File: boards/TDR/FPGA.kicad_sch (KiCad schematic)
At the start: 1 part, among them U1 LFE5UM5G-45-CABGA381

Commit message: change crystal footprint and roughly finish schematic
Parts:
- added U16: LFE5UM5G-25-CABGA381, symbol ECP5:LFE5UM5G-25-CABGA381
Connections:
- net VCCIO7 is gone; now on net +3V3: U1.H6 (VCCIO7), U1.H7 (VCCIO7), U1.J6 (VCCIO7)
- net D0: now also U1.C2 (PL23D)
- net D1: now also U1.B1 (PL23B)
- net D2: now also U1.B2 (PL23C)
- net D3: now also U1.A2 (PL23A)
- net D4: now also U1.B3 (PL14D)
- net D5: now also U1.A3 (PL14C)
- net D6: now also U1.B4 (PL14B)
- net D7: now also U1.A4 (PL11A)
- net RD#: now also U1.C5 (PL11D)
- net RXF#: now also U1.B5 (PL11C)
- net SIWU: now also U1.E5 (PL20C)
- net TXE#: now also U1.A5 (PL11B)
- net WR#: now also U1.D5 (PL17B)

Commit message: connect fpga vccio to 3.3V, add decoupling, route some tracks
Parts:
- removed U16: LFE5UM5G-25-CABGA381, symbol ECP5:LFE5UM5G-25-CABGA381
- added C21, C5: 100n, Capacitor_SMD:C_0402_1005Metric, symbol Device:C
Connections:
- net +3V3: now also C21.1, C5.1
- net GND: now also C21.2, C5.2
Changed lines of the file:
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@@
   (junction (at 53.34 133.35) (diameter 0) (color 0 0 0 0))
   (junction (at 54.61 140.97) (diameter 0) (color 0 0 0 0))
+  (junction (at 55.88 130.81) (diameter 0) (color 0 0 0 0))
   (junction (at 83.82 26.67) (diameter 0) (color 0 0 0 0))
   (junction (at 116.84 29.21) (diameter 0) (color 0 0 0 0))
@@
   (junction (at 185.42 29.21) (diameter 0) (color 0 0 0 0))
   (junction (at 217.17 29.21) (diameter 0) (color 0 0 0 0))
+  (junction (at 220.98 29.21) (diameter 0) (color 0 0 0 0))
   (wire (pts (xy 49.53 26.67) (xy 50.8 26.67))
     (stroke (width 0) (type solid) (color 0 0 0 0))
@@
     (stroke (width 0) (type solid) (color 0 0 0 0))
   )
+  (wire (pts (xy 55.88 130.81) (xy 59.69 130.81))
+    (stroke (width 0) (type solid) (color 0 0 0 0))
+  )
+  (wire (pts (xy 67.31 130.81) (xy 69.85 130.81))
+    (stroke (width 0) (type solid) (color 0 0 0 0))
+  )
+  (wire (pts (xy 69.85 130.81) (xy 69.85 131.445))
+    (stroke (width 0) (type solid) (color 0 0 0 0))
+  )
   (wire (pts (xy 82.55 26.67) (xy 83.82 26.67))
     (stroke (width 0) (type solid) (color 0 0 0 0))
@@
   )
   (wire (pts (xy 220.98 27.94) (xy 220.98 29.21))
+    (stroke (width 0) (type solid) (color 0 0 0 0))
+  )
+  (wire (pts (xy 220.98 29.21) (xy 225.425 29.21))
+    (stroke (width 0) (type solid) (color 0 0 0 0))
+  )
+  (wire (pts (xy 233.045 29.21) (xy 234.315 29.21))
+    (stroke (width 0) (type solid) (color 0 0 0 0))
+  )
+  (wire (pts (xy 234.315 29.21) (xy 234.315 29.845))
     (stroke (width 0) (type solid) (color 0 0 0 0))
   )
@@
     )
     (property "Datasheet" "" (id 3) (at 57.15 140.97 0)
+      (effects (font (size 1.27 1.27)) hide)
+    )
+  )
+  (symbol (lib_id "power:GND") (at 69.85 131.445 0) (unit 1)
+    (in_bom yes) (on_board yes)
+    (property "Reference" "#PWR0144" (id 0) (at 69.85 137.795 0)
+      (effects (font (size 1.27 1.27)) hide)
+    )
+    (property "Value" "GND" (id 1) (at 73.66 132.715 0))
+    (property "Footprint" "" (id 2) (at 69.85 131.445 0)
+      (effects (font (size 1.27 1.27)) hide)
+    )
+    (property "Datasheet" "" (id 3) (at 69.85 131.445 0)
+      (effects (font (size 1.27 1.27)) hide)
+    )
+  )
+  (symbol (lib_id "power:GND") (at 234.315 29.845 0) (unit 1)
+    (in_bom yes) (on_board yes)
+    (property "Reference" "#PWR0143" (id 0) (at 234.315 36.195 0)
+      (effects (font (size 1.27 1.27)) hide)
+    )
+    (property "Value" "GND" (id 1) (at 238.125 31.115 0))
+    (property "Footprint" "" (id 2) (at 234.315 29.845 0)
+      (effects (font (size 1.27 1.27)) hide)
+    )
+    (property "Datasheet" "" (id 3) (at 234.315 29.845 0)
+      (effects (font (size 1.27 1.27)) hide)
+    )
+  )
+  (symbol (lib_id "Device:C") (at 63.5 130.81 90) (unit 1)
+    (in_bom yes) (on_board yes)
+    (property "Reference" "C5" (id 0) (at 63.5 124.4408 90))
+    (property "Value" "100n" (id 1) (at 63.5 126.7395 90))
+    (property "Footprint" "Capacitor_SMD:C_0402_1005Metric" (id 2) (at 67.31 129.8448 0)
+      (effects (font (size 1.27 1.27)) hide)
+    )
+    (property "Datasheet" "~" (id 3) (at 63.5 130.81 0)
+      (effects (font (size 1.27 1.27)) hide)
+    )
+  )
+  (symbol (lib_id "Device:C") (at 229.235 29.21 90) (unit 1)
+    (in_bom yes) (on_board yes)
+    (property "Reference" "C21" (id 0) (at 229.235 22.8408 90))
+    (property "Value" "100n" (id 1) (at 229.235 25.1395 90))
+    (property "Footprint" "Capacitor_SMD:C_0402_1005Metric" (id 2) (at 233.045 28.2448 0)
+      (effects (font (size 1.27 1.27)) hide)
+    )
+    (property "Datasheet" "~" (id 3) (at 229.235 29.21 0)
       (effects (font (size 1.27 1.27)) hide)
     )
@@
     )
   )
-  (symbol (lib_id "ECP5:LFE5UM5G-25-CABGA381") (at 655.32 80.01 0) (unit 10)
-    (in_bom yes) (on_board yes)
-    (property "Reference" "U16" (id 0) (at 646.43 -71.12 0))
-    (property "Value" "LFE5UM5G-25-CABGA381" (id 1) (at 657.86 231.14 0))
-    (property "Footprint" "" (id 2) (at 655.32 80.01 0)
-      (effects (font (size 1.27 1.27)) hide)
-    )
-    (property "Datasheet" "" (id 3) (at 655.32 80.01 0)
-      (effects (font (size 1.27 1.27)) hide)
-    )
-  )
   (symbol (lib_id "ECP5:LFE5UM5G-45-CABGA381") (at 105.41 142.24 0) (unit 5)
     (in_bom yes) (on_board yes)
@@
     )
   )
-  (symbol (lib_id "ECP5:LFE5UM5G-25-CABGA381") (at 513.08 93.345 0) (unit 5)
-    (in_bom yes) (on_board yes)
-    (property "Reference" "U16" (id 0) (at 504.19 -57.785 0))
-    (property "Value" "LFE5UM5G-25-CABGA381" (id 1) (at 515.62 244.475 0))
-    (property "Footprint" "" (id 2) (at 513.08 93.345 0)
-      (effects (font (size 1.27 1.27)) hide)
-    )
-    (property "Datasheet" "" (id 3) (at 513.08 93.345 0)
-      (effects (font (size 1.27 1.27)) hide)
-    )
-  )
   (symbol (lib_id "ECP5:LFE5UM5G-45-CABGA381") (at 154.94 149.225 0) (unit 6)
     (in_bom yes) (on_board yes)
@@
     )
   )
-  (symbol (lib_id "ECP5:LFE5UM5G-25-CABGA381") (at 551.815 80.645 0) (unit 6)
-    (in_bom yes) (on_board yes)
-    (property "Reference" "U16" (id 0) (at 542.925 -70.485 0))
-    (property "Value" "LFE5UM5G-25-CABGA381" (id 1) (at 554.355 231.775 0))
-    (property "Footprint" "" (id 2) (at 551.815 80.645 0)
-      (effects (font (size 1.27 1.27)) hide)
-    )
-    (property "Datasheet" "" (id 3) (at 551.815 80.645 0)
-      (effects (font (size 1.27 1.27)) hide)
-    )
-  )
   (symbol (lib_id "ECP5:LFE5UM5G-45-CABGA381") (at 41.91 157.48 0) (unit 10)
     (in_bom yes) (on_board yes)
@@
     )
   )
-  (symbol (lib_id "ECP5:LFE5UM5G-25-CABGA381") (at 576.58 85.725 0) (unit 9)
-    (in_bom yes) (on_board yes)
-    (property "Reference" "U16" (id 0) (at 567.69 -65.405 0))
-    (property "Value" "LFE5UM5G-25-CABGA381" (id 1) (at 579.12 236.855 0))
-    (property "Footprint" "" (id 2) (at 576.58 85.725 0)
-      (effects (font (size 1.27 1.27)) hide)
-    )
-    (property "Datasheet" "" (id 3) (at 576.58 85.725 0)
-      (effects (font (size 1.27 1.27)) hide)
-    )
-  )
-  (symbol (lib_id "ECP5:LFE5UM5G-25-CABGA381") (at 386.08 86.995 0) (unit 1)
-    (in_bom yes) (on_board yes)
-    (property "Reference" "U16" (id 0) (at 377.19 -64.135 0))
-    (property "Value" "LFE5UM5G-25-CABGA381" (id 1) (at 388.62 238.125 0))
-    (property "Footprint" "" (id 2) (at 386.08 86.995 0)
-      (effects (font (size 1.27 1.27)) hide)
-    )
-    (property "Datasheet" "" (id 3) (at 386.08 86.995 0)
-      (effects (font (size 1.27 1.27)) hide)
-    )
-  )
   (symbol (lib_id "ECP5:LFE5UM5G-45-CABGA381") (at 39.37 63.5 0) (unit 1)
     (in_bom yes) (on_board yes)
@@
     )
   )
-  (symbol (lib_id "ECP5:LFE5UM5G-25-CABGA381") (at 361.95 92.075 0) (unit 2)
-    (in_bom yes) (on_board yes)
-    (property "Reference" "U16" (id 0) (at 353.06 -59.055 0))
-    (property "Value" "LFE5UM5G-25-CABGA381" (id 1) (at 364.49 243.205 0))
-    (property "Footprint" "" (id 2) (at 361.95 92.075 0)
-      (effects (font (size 1.27 1.27)) hide)
-    )
-    (property "Datasheet" "" (id 3) (at 361.95 92.075 0)
-      (effects (font (size 1.27 1.27)) hide)
-    )
-  )
   (symbol (lib_id "ECP5:LFE5UM5G-45-CABGA381") (at 72.39 71.12 0) (unit 2)
     (in_bom yes) (on_board yes)
@@
       (effects (font (size 1.27 1.27)) hide)
     )
-  )
-  (symbol (lib_id "ECP5:LFE5UM5G-25-CABGA381") (at 407.035 93.98 0) (unit 3)
-    (in_bom yes) (on_board yes)
-    (property "Reference" "U16" (id 0) (at 398.145 -57.15 0))
-    (property "Value" "LFE5UM5G-25-CABGA381" (id 1) (at 409.575 245.11 0))
-    (property "Footprint" "" (id 2) (at 407.035 93.98 0)
-      (effects (font (size 1.27 1.27)) hide)
-    )
-    (property "Datasheet" "" (id 3) (at 407.035 93.98 0)
-      (effects (font (size 1.27 1.27)) hide)
-    )
-  )
-  (symbol (lib_id "ECP5:LFE5UM5G-25-CABGA381") (at 423.545 93.98 0) (unit 4)
-    (in_bom yes) (on_board yes)
-    (property "Reference" "U16" (id 0) (at 414.655 -57.15 0))
-    (property "Value" "LFE5UM5G-25-CABGA381" (id 1) (at 426.085 245.11 0))
-    (property "Footprint" "" (id 2) (at 423.545 93.98 0)
-      (effects (font (size 1.27 1.27)) hide)
-    )
-    (property "Datasheet" "" (id 3) (at 423.545 93.98 0)
-      (effects (font (size 1.27 1.27)) hide)
-    )
-  )
-  (symbol (lib_id "ECP5:LFE5UM5G-25-CABGA381") (at 447.04 94.615 0) (unit 7)
-    (in_bom yes) (on_board yes)
-    (property "Reference" "U16" (id 0) (at 438.15 -56.515 0))
-    (property "Value" "LFE5UM5G-25-CABGA381" (id 1) (at 449.58 245.745 0))
-    (property "Footprint" "" (id 2) (at 447.04 94.615 0)
-      (effects (font (size 1.27 1.27)) hide)
-    )
-    (property "Datasheet" "" (id 3) (at 447.04 94.615 0)
-      (effects (font (size 1.27 1.27)) hide)
-    )
-  )
-  (symbol (lib_id "ECP5:LFE5UM5G-25-CABGA381") (at 473.71 86.36 0) (unit 8)
-    (in_bom yes) (on_board yes)
-    (property "Reference" "U16" (id 0) (at 464.82 -64.77 0))
-    (property "Value" "LFE5UM5G-25-CABGA381" (id 1) (at 476.25 237.49 0))
-    (property "Footprint" "" (id 2) (at 473.71 86.36 0)
-      (effects (font (size 1.27 1.27)) hide)
-    )
-    (property "Datasheet" "" (id 3) (at 473.71 86.36 0)
-      (effects (font (size 1.27 1.27)) hide)
-    )

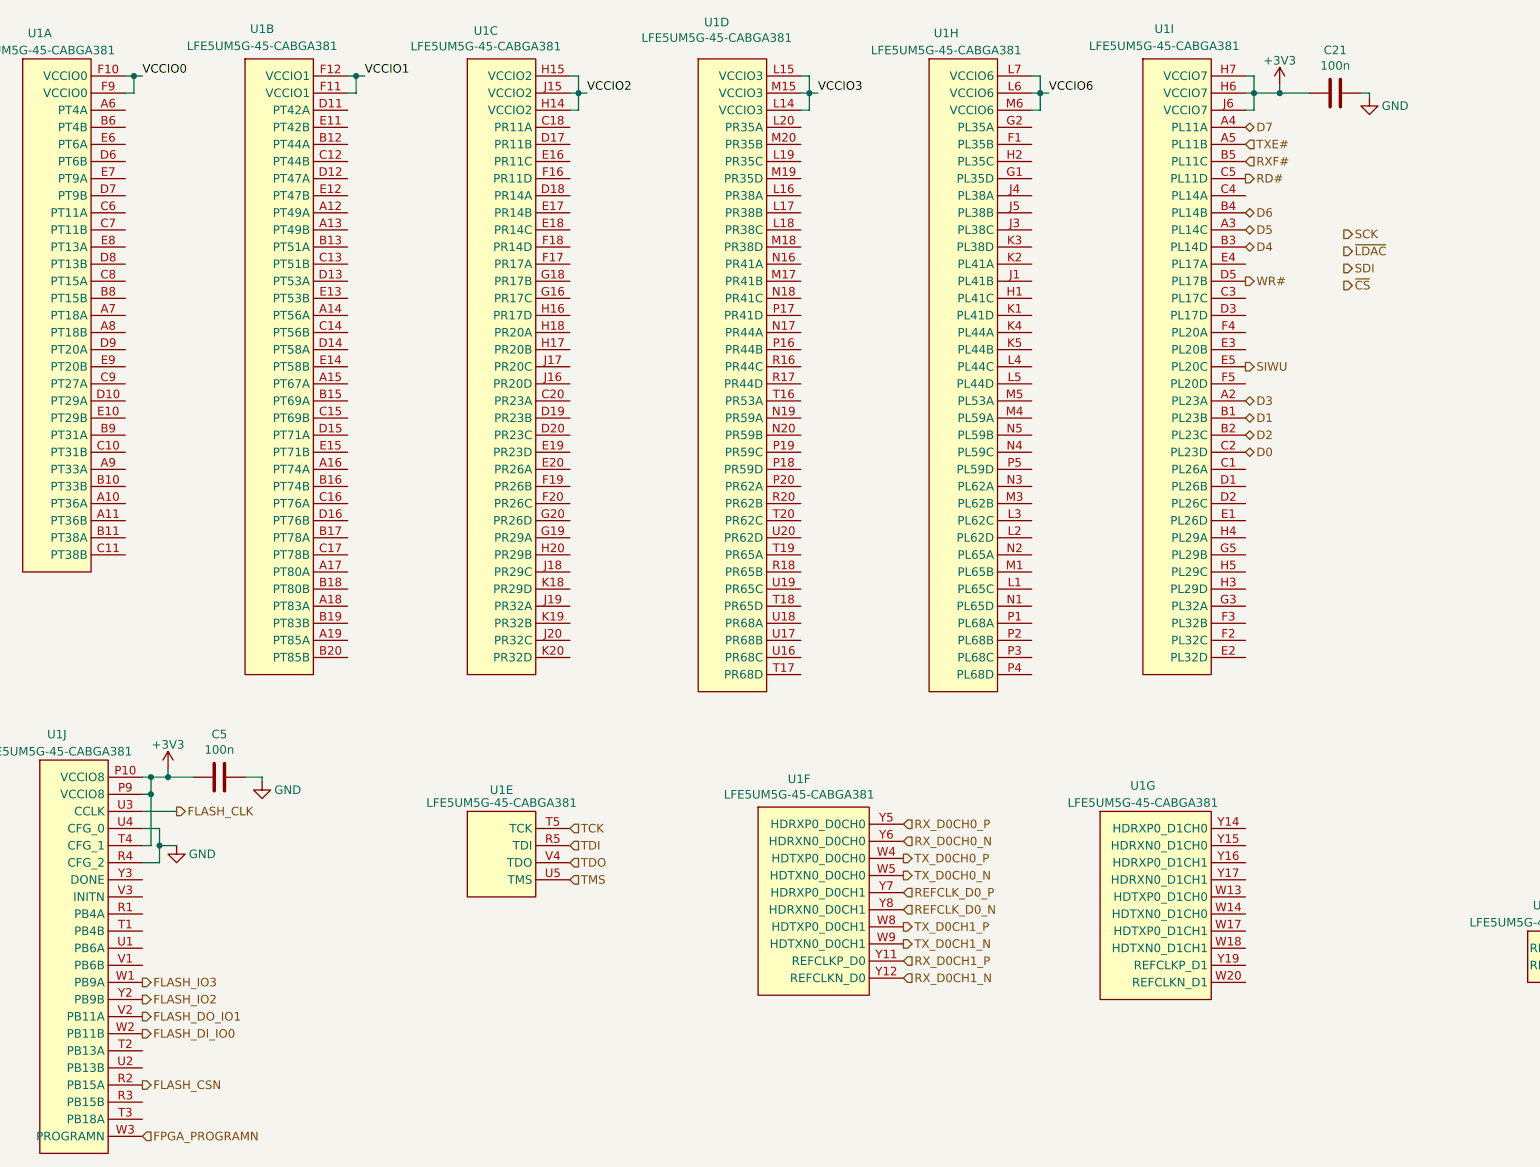
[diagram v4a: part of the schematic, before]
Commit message: solved DRC errors and routed few more nets
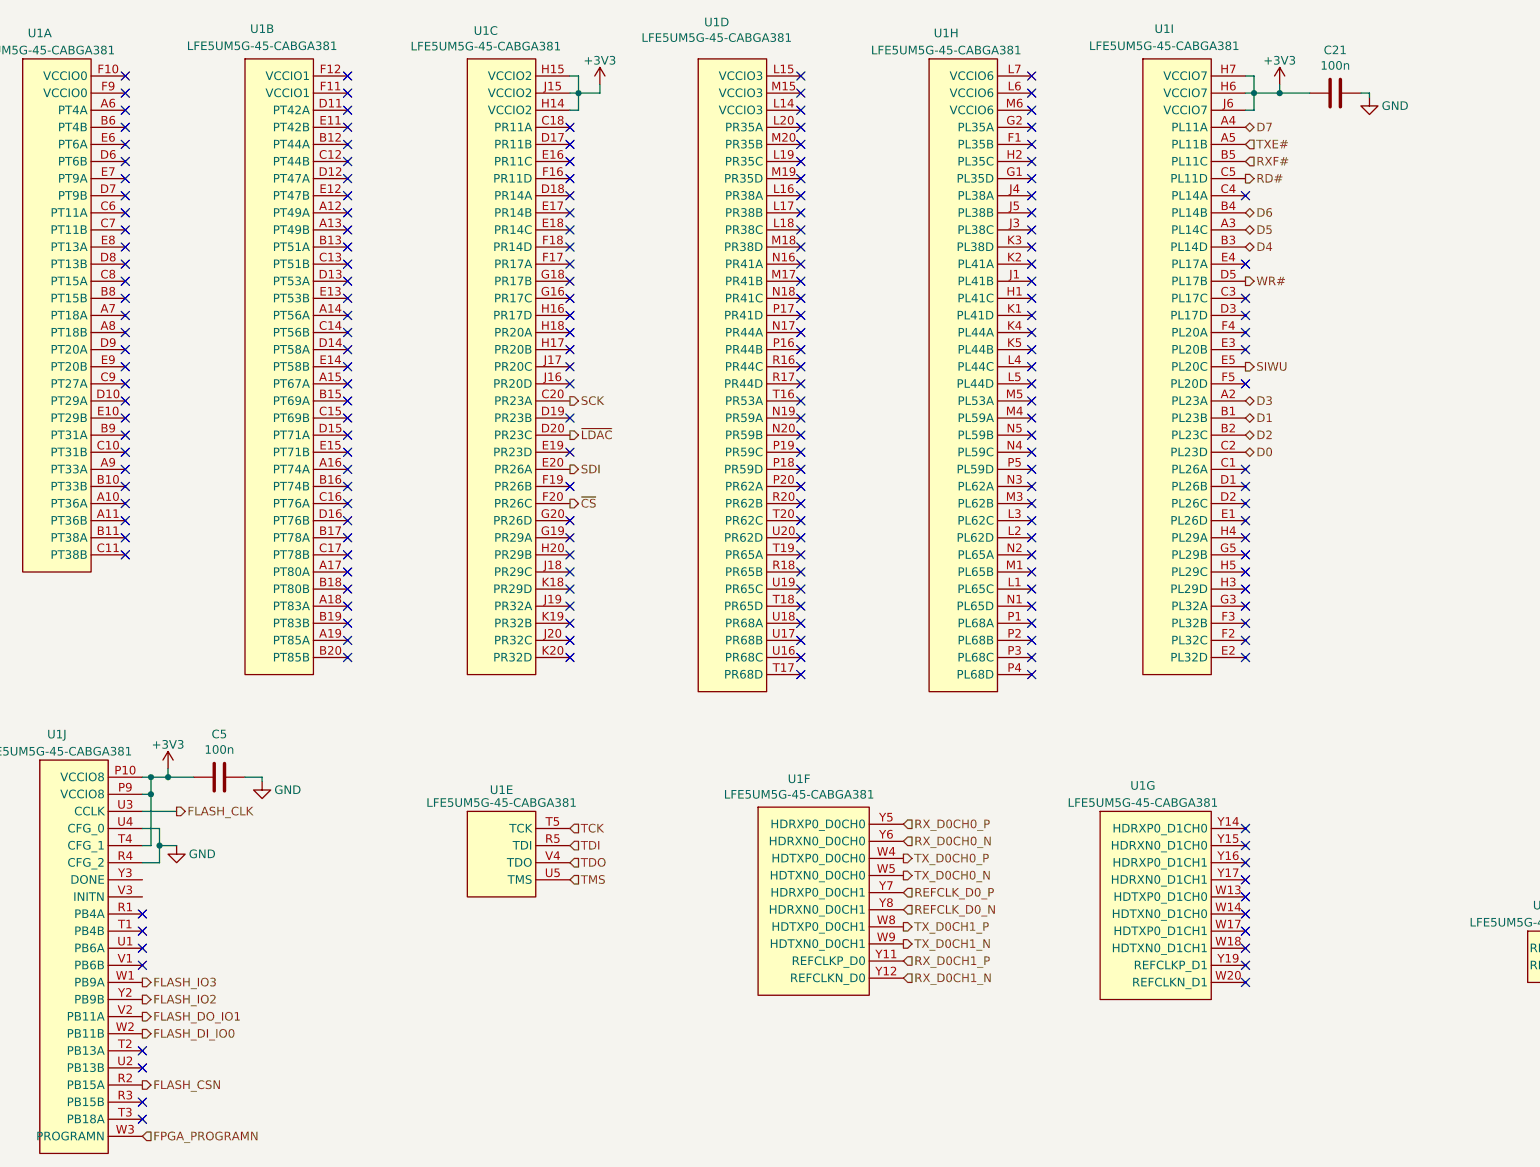
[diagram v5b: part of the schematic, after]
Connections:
- net VCCIO2 is gone; now on net +3V3: U1.H14 (VCCIO2), U1.H15 (VCCIO2), U1.J15 (VCCIO2)
- net SCK: now also U1.C20 (PR23A)
- net SDI: now also U1.E20 (PR26A)
- net ~CS: now also U1.F20 (PR26C)
- net ~LDAC: now also U1.D20 (PR23C)
- net VCCIO0: no longer names the net of U1.F10 (VCCIO0)
- net VCCIO0: no longer U1.F9 (VCCIO0)
- net VCCIO1: no longer names the net of U1.F11 (VCCIO1)
- net VCCIO1: no longer U1.F12 (VCCIO1)
- removed net VCCIO3: U1.L14 (VCCIO3), U1.L15 (VCCIO3), U1.M15 (VCCIO3)
- removed net VCCIO6: U1.L6 (VCCIO6), U1.L7 (VCCIO6), U1.M6 (VCCIO6)
- no-connect marks 0 -> 201
